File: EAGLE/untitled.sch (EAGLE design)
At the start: 55 parts, among them IC1 MIC29302WU, IC3 FT231XS-R, IC6 SMF05CT2G, J13 693023010811, Q1 MMBT3904, Q6 MMBT3904-TP, Q7 MMBT3904-TP, U6 SI2301BDS-T1-E3, X1 04-JST-B4B-XH-A

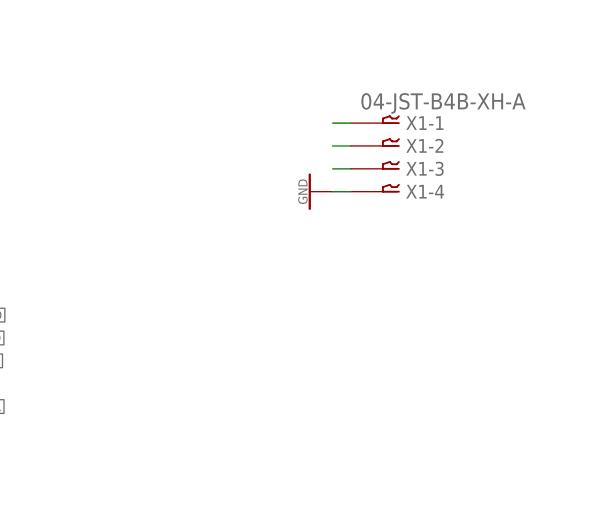
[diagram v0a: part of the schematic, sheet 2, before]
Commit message: FEAT: add connector to mcu
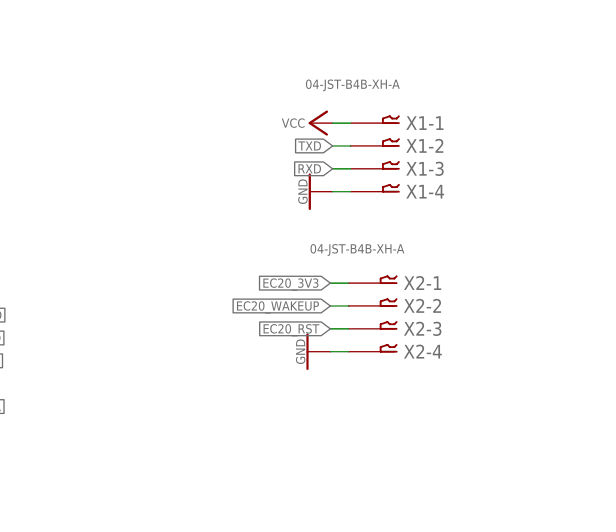
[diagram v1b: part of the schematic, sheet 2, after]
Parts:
- added X2: 04-JST-B4B-XH-A, AccesControlNFC:04-JST-B4B-XH-A
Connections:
- removed net N$8: X1-2.1
- removed net N$9: X1-3.1
- net EC20_3V3: now also X2-1.1
- net EC20_RST: now also X2-3.1
- net EC20_WAKEUP: now also X2-2.1
- net GND: now also X2-4.1
- net N$7: now also LED2.A, R8.1; no longer X1-1.1
- net RXD: now also X1-3.1
- net TXD: now also X1-2.1
- net VCC: now also X1-1.1
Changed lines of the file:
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@@
 <part name="X1" library="AccesControlNFC" library_urn="urn:adsk.eagle:library:37185839" deviceset="04-JST" device="-B4B-XH-A" package3d_urn="urn:adsk.eagle:package:37185910/1"/>
 <part name="GND9" library="DecawaveLibrary" library_urn="urn:adsk.eagle:library:5224885" deviceset="GND" device=""/>
+<part name="P+4" library="supply1" library_urn="urn:adsk.eagle:library:371" deviceset="VCC" device=""/>
+<part name="X2" library="AccesControlNFC" library_urn="urn:adsk.eagle:library:37185839" deviceset="04-JST" device="-B4B-XH-A" package3d_urn="urn:adsk.eagle:package:37185910/1"/>
+<part name="GND16" library="DecawaveLibrary" library_urn="urn:adsk.eagle:library:5224885" deviceset="GND" device=""/>
 </parts>
 <sheets>
@@
 </segment>
 </net>
+<net name="N$7" class="0">
+<segment>
+<pinref part="LED2" gate="G$1" pin="A"/>
+<pinref part="R8" gate="G$1" pin="1"/>
+<wire x1="217.932" y1="162.56" x2="218.44" y2="162.56" width="0.1524" layer="91"/>
+</segment>
+</net>
 </nets>
 </sheet>
@@
 <instance part="X1" gate="-1" x="214.122" y="129.286" smashed="yes">
 <attribute name="NAME" x="215.138" y="128.524" size="1.524" layer="95"/>
-<attribute name="VALUE" x="210.058" y="130.81" size="1.778" layer="96"/>
+<attribute name="VALUE" x="203.962" y="133.096" size="1.016" layer="96"/>
 </instance>
 <instance part="X1" gate="-2" x="214.122" y="126.746" smashed="yes">
@@
 <instance part="GND9" gate="1" x="204.47" y="121.666" smashed="yes" rot="R270">
 <attribute name="VALUE" x="204.216" y="121.666" size="1.016" layer="96" rot="R270" align="top-center"/>
+</instance>
+<instance part="P+4" gate="VCC" x="204.47" y="129.286" smashed="yes" rot="R90">
+<attribute name="VALUE" x="203.962" y="129.794" size="1.016" layer="96" rot="R180"/>
+</instance>
+<instance part="X2" gate="-1" x="213.868" y="111.506" smashed="yes">
+<attribute name="NAME" x="214.884" y="110.744" size="1.524" layer="95"/>
+<attribute name="VALUE" x="204.47" y="114.808" size="1.016" layer="96"/>
+</instance>
+<instance part="X2" gate="-2" x="213.868" y="108.966" smashed="yes">
+<attribute name="NAME" x="214.884" y="108.204" size="1.524" layer="95"/>
+</instance>
+<instance part="X2" gate="-3" x="213.868" y="106.426" smashed="yes">
+<attribute name="NAME" x="214.884" y="105.664" size="1.524" layer="95"/>
+</instance>
+<instance part="X2" gate="-4" x="213.868" y="103.886" smashed="yes">
+<attribute name="NAME" x="214.884" y="103.124" size="1.524" layer="95"/>
+</instance>
+<instance part="GND16" gate="1" x="204.216" y="103.886" smashed="yes" rot="R270">
+<attribute name="VALUE" x="203.962" y="103.886" size="1.016" layer="96" rot="R270" align="top-center"/>
 </instance>
 </instances>
@@
 <wire x1="209.042" y1="121.666" x2="207.01" y2="121.666" width="0.1524" layer="91"/>
 <pinref part="GND9" gate="1" pin="GND"/>
+</segment>
+<segment>
+<pinref part="X2" gate="-4" pin="1"/>
+<wire x1="208.788" y1="103.886" x2="206.756" y2="103.886" width="0.1524" layer="91"/>
+<pinref part="GND16" gate="1" pin="GND"/>
 </segment>
 </net>
@@
 <label x="166.37" y="105.41" size="1.016" layer="95" xref="yes"/>
 </segment>
+<segment>
+<pinref part="X1" gate="-2" pin="1"/>
+<wire x1="209.042" y1="126.746" x2="207.01" y2="126.746" width="0.1524" layer="91"/>
+<label x="207.01" y="126.746" size="1.016" layer="95" rot="R180" xref="yes"/>
+</segment>
 </net>
 <net name="RXD" class="0">
@@
 <wire x1="163.83" y1="107.95" x2="166.37" y2="107.95" width="0.1524" layer="91"/>
 <label x="166.37" y="107.95" size="1.016" layer="95" xref="yes"/>
+</segment>
+<segment>
+<pinref part="X1" gate="-3" pin="1"/>
+<wire x1="209.042" y1="124.206" x2="207.01" y2="124.206" width="0.1524" layer="91"/>
+<label x="207.01" y="124.206" size="1.016" layer="95" rot="R180" xref="yes"/>
 </segment>
 </net>
@@
 </segment>
 </net>
-<net name="N$7" class="0">
+<net name="VCC" class="0">
 <segment>
 <pinref part="X1" gate="-1" pin="1"/>
 <wire x1="209.042" y1="129.286" x2="207.01" y2="129.286" width="0.1524" layer="91"/>
-</segment>
-</net>
-<net name="N$8" class="0">
-<segment>
-<pinref part="X1" gate="-2" pin="1"/>
-<wire x1="209.042" y1="126.746" x2="207.01" y2="126.746" width="0.1524" layer="91"/>
-</segment>
-</net>
-<net name="N$9" class="0">
-<segment>
-<pinref part="X1" gate="-3" pin="1"/>
-<wire x1="209.042" y1="124.206" x2="207.01" y2="124.206" width="0.1524" layer="91"/>
-</segment>
-</net>
+<pinref part="P+4" gate="VCC" pin="VCC"/>
+</segment>
+</net>
+<net name="EC20_3V3" class="0">
+<segment>
+<pinref part="X2" gate="-1" pin="1"/>
+<wire x1="208.788" y1="111.506" x2="206.756" y2="111.506" width="0.1524" layer="91"/>
+<label x="206.756" y="111.506" size="1.016" layer="95" rot="R180" xref="yes"/>
+</segment>
+</net>
+<net name="EC20_WAKEUP" class="0">
+<segment>
+<pinref part="X2" gate="-2" pin="1"/>
+<wire x1="208.788" y1="108.966" x2="206.756" y2="108.966" width="0.1524" layer="91"/>
+<label x="206.756" y="108.966" size="1.016" layer="95" rot="R180" xref="yes"/>
+</segment>
+</net>
+<net name="EC20_RST" class="0">
+<segment>
+<pinref part="X2" gate="-3" pin="1"/>
+<wire x1="208.788" y1="106.426" x2="206.756" y2="106.426" width="0.1524" layer="91"/>
+<label x="206.756" y="106.426" size="1.016" layer="95" rot="R180" xref="yes"/>
+</segment>
+</net>

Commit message: FEAT: update layout pcb
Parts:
- removed Q6, Q7: MMBT3904-TP, AccesControlNFC:MMBT3904-TP
- removed R11, R12: 10k, AccesControlNFC:ESR03EZPJ103
- removed R127, R94: 10r, ERJ-3EKF10R0V:ERJ-3EKF10R0V
- removed R193: 50, RT0603BRE0750RL:RT0603BRE0750RL
- added H1, H2, H3, H4, H5, H6: 3MM_HOLE, 3mm_special_hole:3MM_HOLE
- added PSU_EN: (no value), pinhead:PINHD-1X2
- renumbered EC25/EC20 to MODEM, X1 to SERIALMCU, X2 to IO_MODEM
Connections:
- removed net EN: Q7.C
- removed net IO0: R193.2
- removed net N$137: Q6.C, R193.1
- removed net N$16: Q7.B, R11.2
- removed net N$17: Q6.B, R12.2
- removed net _D+: R127.2
- removed net _D-: R94.2
- net D+: no longer R127.1
- net D-: no longer R94.1
- net DTR: no longer Q6.E, R11.1
- net GND: now also PSU_EN.2
- net RST: now also PSU_EN.1
- net RTS: no longer Q7.E, R12.1

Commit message: FEAT: update route pcb
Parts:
- added JP1, JP2: (no value), pinhead:PINHD-1X3
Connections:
- new net D+_IC: IC3.USBDP, JP1.1
- new net D+_USB: JP1.3, USB.DP1, USB.DP2
- new net D-_IC: IC3.USBDM, JP2.1
- new net D-_USB: JP2.3, USB.DN1, USB.DN2
- net D+: now also JP1.2; no longer USB.DP1, USB.DP2
- net D-: now also JP2.2; no longer USB.DN1, USB.DN2
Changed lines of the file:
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@@
 <part name="H5" library="3mm_special_hole" library_urn="urn:adsk.eagle:library:36448710" deviceset="3MM_HOLE" device="" package3d_urn="urn:adsk.eagle:package:36448714/1"/>
 <part name="H6" library="3mm_special_hole" library_urn="urn:adsk.eagle:library:36448710" deviceset="3MM_HOLE" device="" package3d_urn="urn:adsk.eagle:package:36448714/1"/>
+<part name="JP1" library="pinhead" library_urn="urn:adsk.eagle:library:325" deviceset="PINHD-1X3" device="" package3d_urn="urn:adsk.eagle:package:22458/2"/>
+<part name="JP2" library="pinhead" library_urn="urn:adsk.eagle:library:325" deviceset="PINHD-1X3" device="" package3d_urn="urn:adsk.eagle:package:22458/2"/>
 </parts>
 <sheets>
@@
 <attribute name="VALUE" x="227.076" y="100.584" size="1.016" layer="96" rot="R270"/>
 </instance>
+<instance part="JP1" gate="A" x="39.624" y="30.734" smashed="yes" rot="R270">
+<attribute name="NAME" x="45.339" y="37.084" size="1.778" layer="95" rot="R270"/>
+<attribute name="VALUE" x="32.004" y="37.084" size="1.778" layer="96" rot="R270"/>
+</instance>
+<instance part="JP2" gate="A" x="68.834" y="30.226" smashed="yes" rot="R270">
+<attribute name="NAME" x="74.549" y="36.576" size="1.778" layer="95" rot="R270"/>
+<attribute name="VALUE" x="61.214" y="36.576" size="1.778" layer="96" rot="R270"/>
+</instance>
 </instances>
 <busses>
@@
 <net name="D-" class="0">
 <segment>
-<wire x1="15.24" y1="60.198" x2="13.462" y2="60.198" width="0.1524" layer="91"/>
-<label x="13.462" y="60.198" size="1.016" layer="95" rot="R180" xref="yes"/>
-<pinref part="USB" gate="G$1" pin="DN1"/>
-</segment>
-<segment>
-<wire x1="50.8" y1="62.738" x2="52.578" y2="62.738" width="0.1524" layer="91"/>
-<label x="52.578" y="62.738" size="1.016" layer="95" xref="yes"/>
-<pinref part="USB" gate="G$1" pin="DN2"/>
-</segment>
-<segment>
 <pinref part="R56" gate="G$1" pin="2"/>
 <wire x1="72.644" y1="139.954" x2="73.406" y2="139.954" width="0.1524" layer="91"/>
 <label x="73.406" y="139.954" size="1.016" layer="95" xref="yes"/>
 </segment>
+<segment>
+<wire x1="68.834" y1="32.766" x2="68.834" y2="37.084" width="0.1524" layer="91"/>
+<label x="68.834" y="37.084" size="1.016" layer="95" rot="R90" xref="yes"/>
+<pinref part="JP2" gate="A" pin="2"/>
+</segment>
 </net>
 <net name="D+" class="0">
-<segment>
-<wire x1="15.24" y1="62.738" x2="13.462" y2="62.738" width="0.1524" layer="91"/>
-<label x="13.462" y="62.738" size="1.016" layer="95" rot="R180" xref="yes"/>
-<pinref part="USB" gate="G$1" pin="DP1"/>
-</segment>
-<segment>
-<wire x1="50.8" y1="60.198" x2="52.578" y2="60.198" width="0.1524" layer="91"/>
-<label x="52.578" y="60.198" size="1.016" layer="95" xref="yes"/>
-<pinref part="USB" gate="G$1" pin="DP2"/>
-</segment>
 <segment>
 <pinref part="R63" gate="G$1" pin="2"/>
 <wire x1="72.39" y1="134.874" x2="73.406" y2="134.874" width="0.1524" layer="91"/>
 <label x="73.406" y="134.874" size="1.016" layer="95" xref="yes"/>
+</segment>
+<segment>
+<wire x1="39.624" y1="33.274" x2="39.624" y2="37.846" width="0.1524" layer="91"/>
+<label x="39.624" y="37.846" size="1.016" layer="95" rot="R90" xref="yes"/>
+<pinref part="JP1" gate="A" pin="2"/>
 </segment>
 </net>
@@
 <pinref part="R8" gate="G$1" pin="1"/>
 <wire x1="217.932" y1="162.56" x2="218.44" y2="162.56" width="0.1524" layer="91"/>
+</segment>
+</net>
+<net name="D+_IC" class="0">
+<segment>
+<wire x1="42.164" y1="33.274" x2="42.164" y2="37.846" width="0.1524" layer="91"/>
+<label x="42.164" y="37.846" size="1.016" layer="95" rot="R90" xref="yes"/>
+<pinref part="JP1" gate="A" pin="1"/>
+</segment>
+</net>
+<net name="D-_IC" class="0">
+<segment>
+<wire x1="71.374" y1="32.766" x2="71.374" y2="36.83" width="0.1524" layer="91"/>
+<label x="71.374" y="36.83" size="1.016" layer="95" rot="R90" xref="yes"/>
+<pinref part="JP2" gate="A" pin="1"/>
+</segment>
+</net>
+<net name="D-_USB" class="0">
+<segment>
+<wire x1="50.8" y1="62.738" x2="52.578" y2="62.738" width="0.1524" layer="91"/>
+<label x="52.578" y="62.738" size="1.016" layer="95" xref="yes"/>
+<pinref part="USB" gate="G$1" pin="DN2"/>
+</segment>
+<segment>
+<wire x1="15.24" y1="60.198" x2="13.462" y2="60.198" width="0.1524" layer="91"/>
+<label x="13.462" y="60.198" size="1.016" layer="95" rot="R180" xref="yes"/>
+<pinref part="USB" gate="G$1" pin="DN1"/>
+</segment>
+<segment>
+<wire x1="66.294" y1="32.766" x2="66.294" y2="37.084" width="0.1524" layer="91"/>
+<label x="66.294" y="37.084" size="1.016" layer="95" rot="R90" xref="yes"/>
+<pinref part="JP2" gate="A" pin="3"/>
+</segment>
+</net>
+<net name="D+_USB" class="0">
+<segment>
+<wire x1="50.8" y1="60.198" x2="52.578" y2="60.198" width="0.1524" layer="91"/>
+<label x="52.578" y="60.198" size="1.016" layer="95" xref="yes"/>
+<pinref part="USB" gate="G$1" pin="DP2"/>
+</segment>
+<segment>
+<wire x1="15.24" y1="62.738" x2="13.462" y2="62.738" width="0.1524" layer="91"/>
+<label x="13.462" y="62.738" size="1.016" layer="95" rot="R180" xref="yes"/>
+<pinref part="USB" gate="G$1" pin="DP1"/>
+</segment>
+<segment>
+<wire x1="37.084" y1="33.274" x2="37.084" y2="37.846" width="0.1524" layer="91"/>
+<label x="37.084" y="37.846" size="1.016" layer="95" rot="R90" xref="yes"/>
+<pinref part="JP1" gate="A" pin="3"/>
 </segment>
 </net>
@@
 </segment>
 </net>
+<net name="D-_IC" class="0">
+<segment>
+<pinref part="IC3" gate="G$1" pin="USBDM"/>
+<wire x1="130.81" y1="102.87" x2="129.286" y2="102.87" width="0.1524" layer="91"/>
+<label x="129.286" y="102.87" size="1.016" layer="95" rot="R180" xref="yes"/>
+</segment>
+</net>
+<net name="D+_IC" class="0">
+<segment>
+<pinref part="IC3" gate="G$1" pin="USBDP"/>
+<wire x1="130.81" y1="100.33" x2="129.286" y2="100.33" width="0.1524" layer="91"/>
+<label x="129.286" y="100.33" size="1.016" layer="95" rot="R180" xref="yes"/>
+</segment>
+</net>
